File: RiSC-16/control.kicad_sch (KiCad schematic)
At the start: 4 parts, among them U16 74LS161, U17 74LS257, U18 74LS283

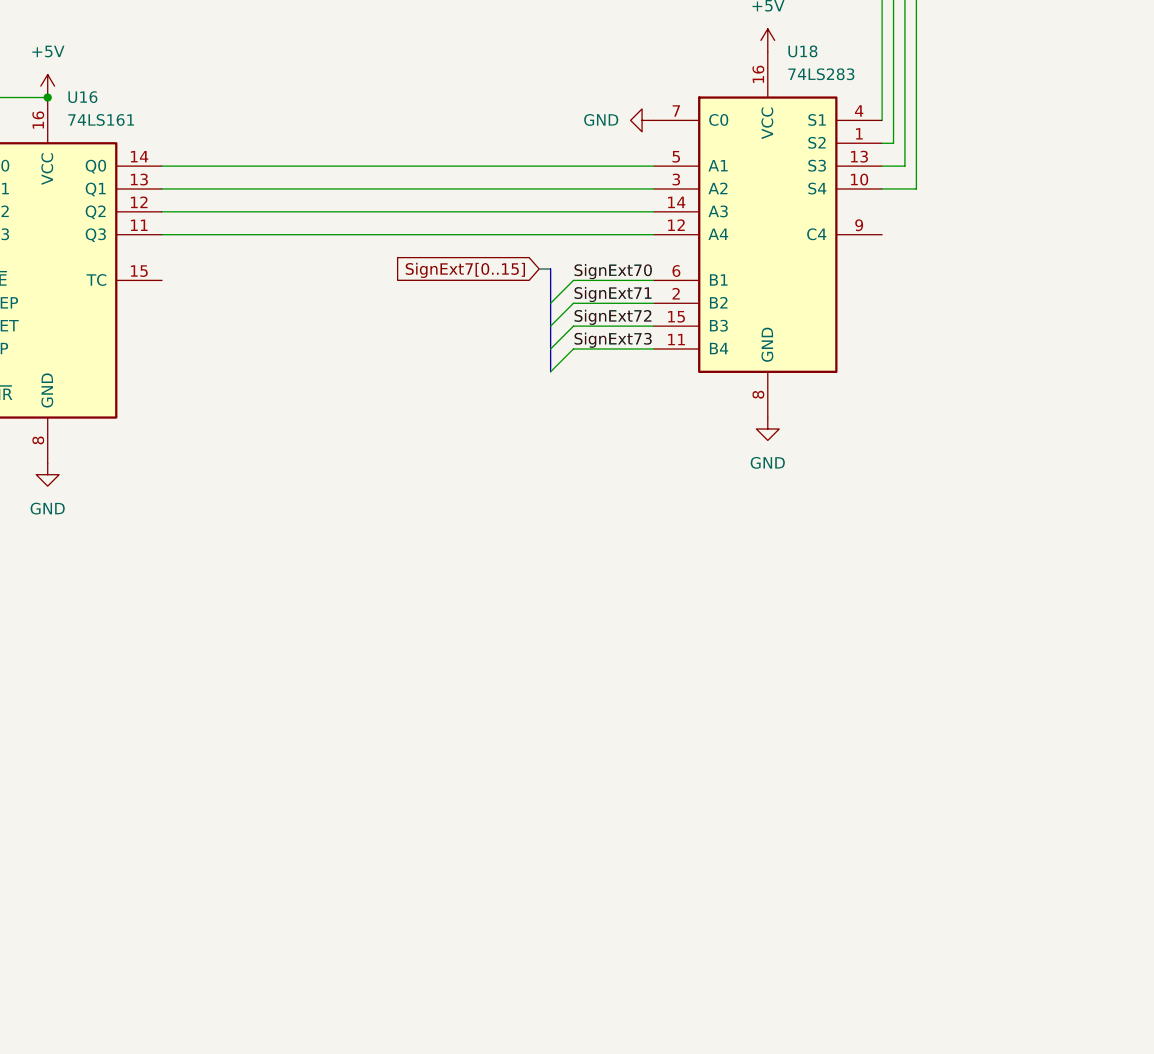
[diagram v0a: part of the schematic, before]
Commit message: Added program counter page.
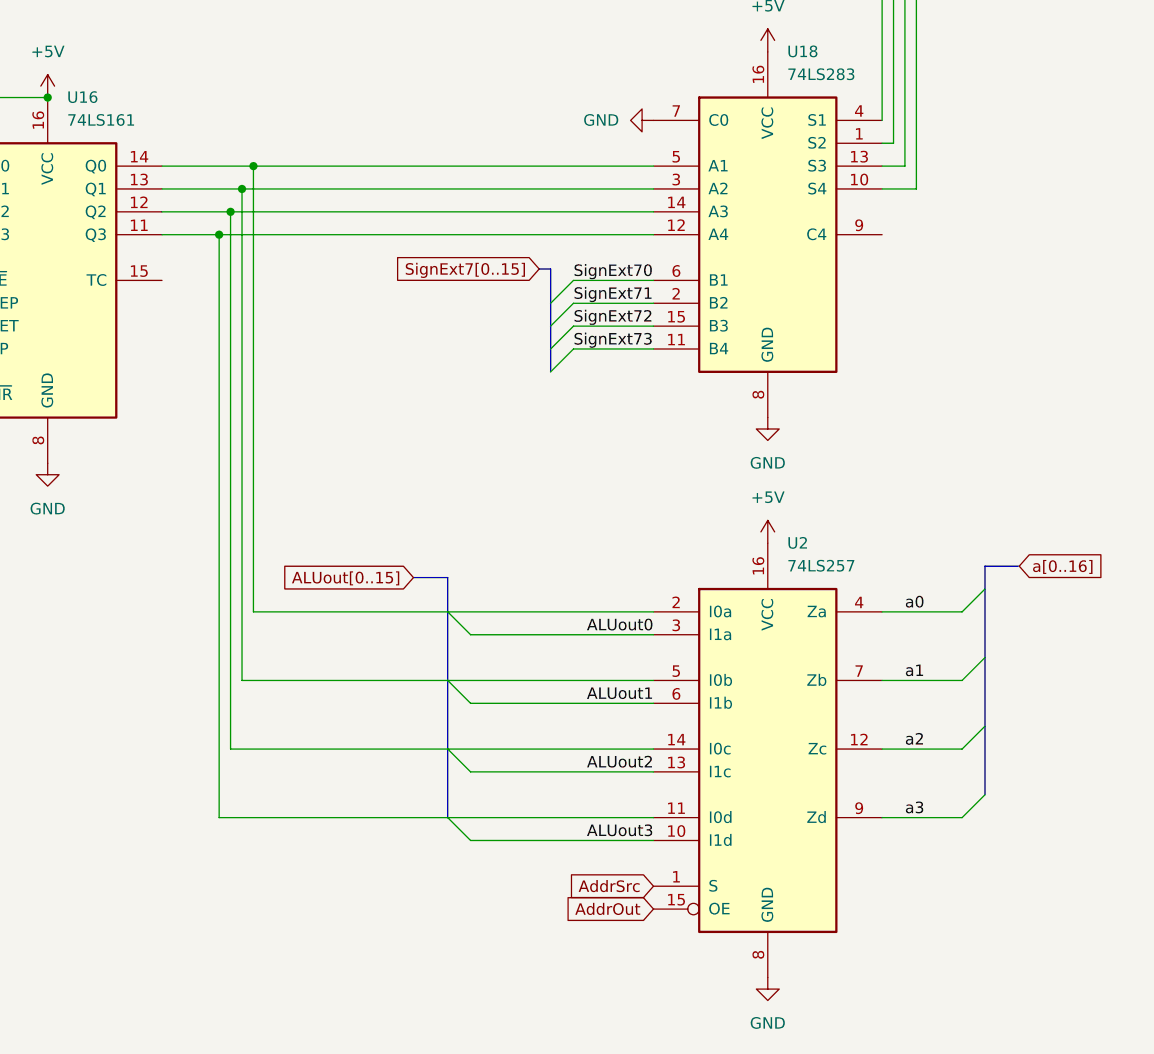
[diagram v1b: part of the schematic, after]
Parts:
- added U2: 74LS257, symbol 74xx:74LS257
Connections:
- net +5V: now also U2.16 (VCC)
- net ALUout0: now also U2.3 (I1a)
- net ALUout1: now also U2.6 (I1b)
- net ALUout2: now also U2.13 (I1c)
- net ALUout3: now also U2.10 (I1d)
- net GND: now also U2.8 (GND)
- net at U16.11 (Q3), U18.12 (A4): now also U2.11 (I0d)
- net at U16.12 (Q2), U18.14 (A3): now also U2.14 (I0c)
- net at U16.13 (Q1), U18.3 (A2): now also U2.5 (I0b)
- net at U16.14 (Q0), U18.5 (A1): now also U2.2 (I0a)
- new net AddrOut: U2.15 (OE)
- new net AddrSrc: U2.1 (S)
- new net a0: U2.4 (Za)
- new net a1: U2.7 (Zb)
- new net a2: U2.12 (Zc)
- new net a3: U2.9 (Zd)

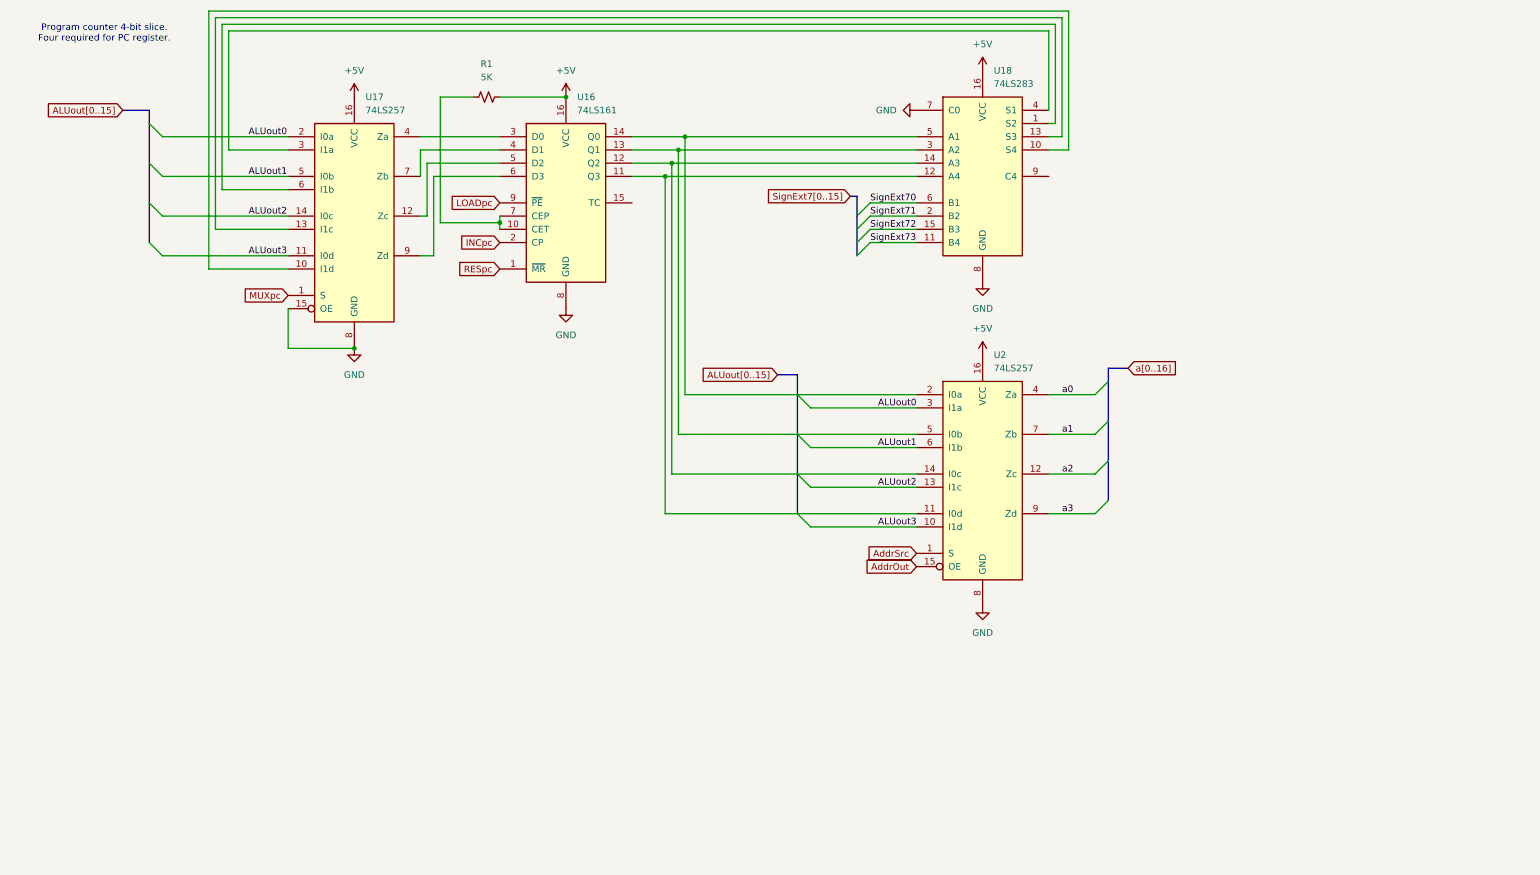
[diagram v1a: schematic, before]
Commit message: Move program ccounter to its own page
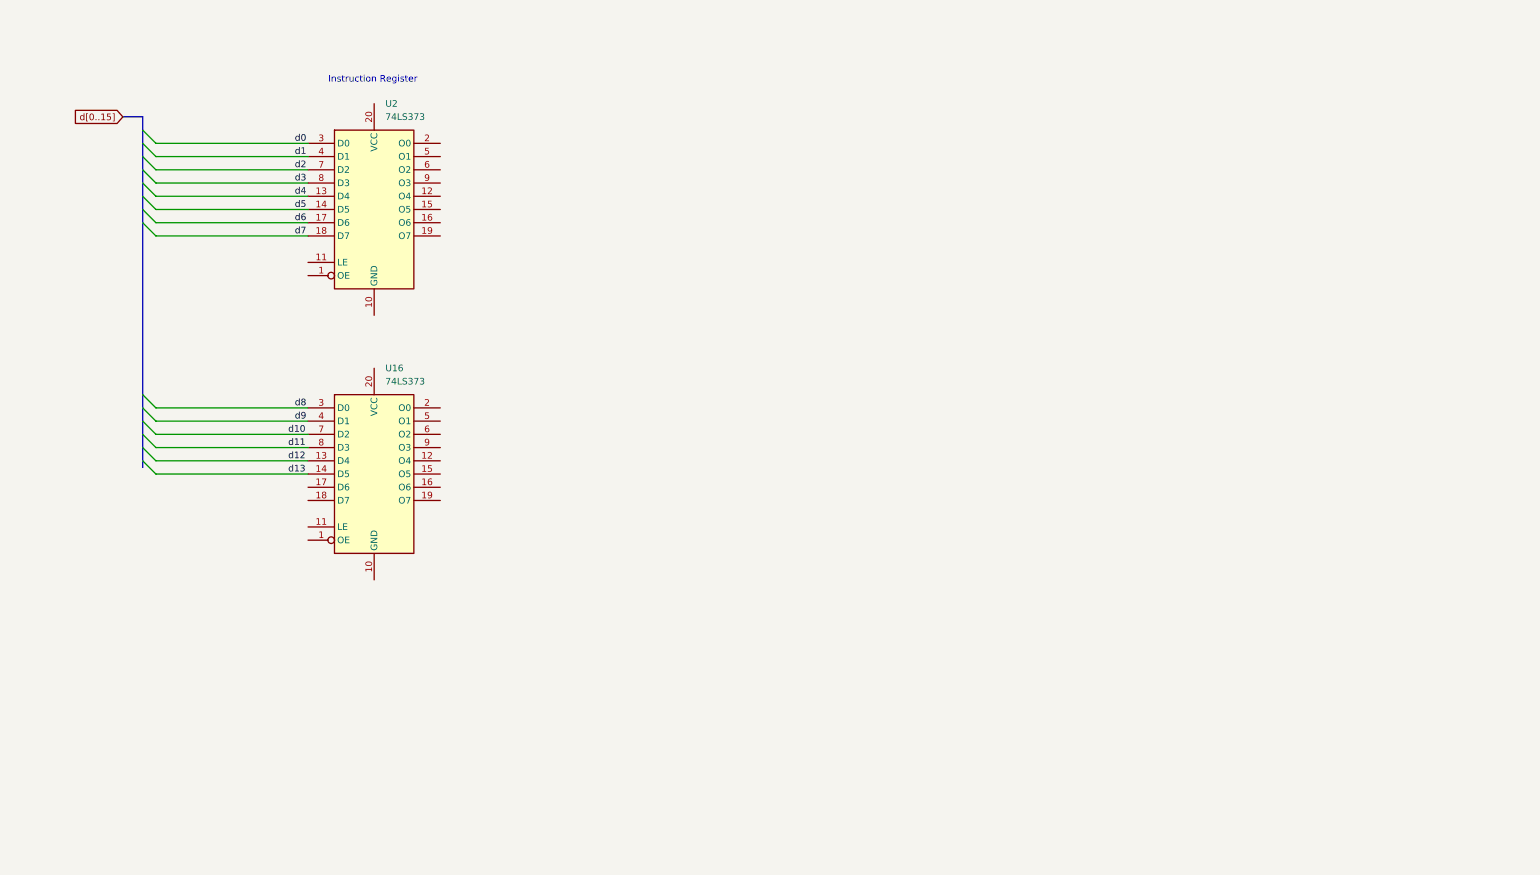
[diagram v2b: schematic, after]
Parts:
- removed R1: 5K, symbol Device:R_Small_US
- removed U16: 74LS161, symbol 74xx:74LS161
- removed U17, U2: 74LS257, symbol 74xx:74LS257
- removed U18: 74LS283, symbol 74xx:74LS283
- added U16, U2: 74LS373, symbol 74xx:74LS373
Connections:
- new net d0: U2.3 (D0)
- new net d1: U2.4 (D1)
- new net d10: U16.7 (D2)
- new net d11: U16.8 (D3)
- new net d12: U16.13 (D4)
- new net d13: U16.14 (D5)
- new net d2: U2.7 (D2)
- new net d3: U2.8 (D3)
- new net d4: U2.13 (D4)
- new net d5: U2.14 (D5)
- new net d6: U2.17 (D6)
- new net d7: U2.18 (D7)
- new net d8: U16.3 (D0)
- new net d9: U16.4 (D1)
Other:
- note added: "Instruction Register"
- note removed: "Program counter 4-bit slice. Four required for PC register."

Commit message: Added instruction register design.
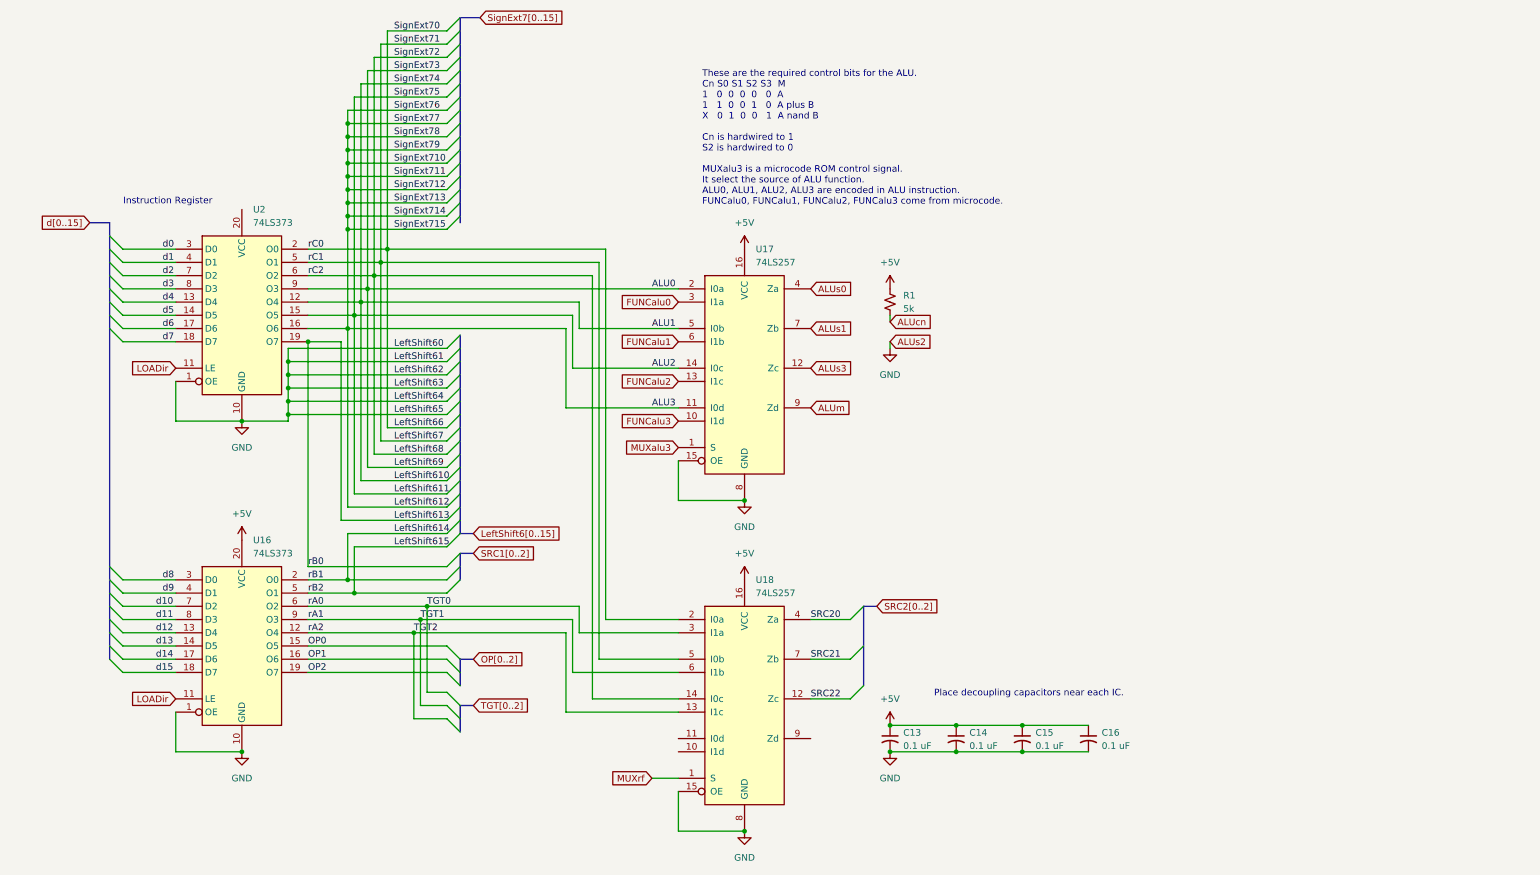
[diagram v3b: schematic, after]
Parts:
- added C13, C14, C15, C16: 0.1 uF, symbol Device:C_Small_US
- added R1: 5k, symbol Device:R_Small_US
- added U17, U18: 74LS257, symbol 74xx:74LS257
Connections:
- net GND: now reaches U16.1 (OE)
- net GND: now also U16.10 (GND), U2.1 (OE), U2.10 (GND), C13.2, C14.2, C15.2, C16.2, U17.15 (OE), U17.8 (GND), U18.15 (OE), U18.8 (GND)
- net LOADir: now reaches U16.11 (LE)
- net LOADir: now also U2.11 (LE)
- net TGT2: now reaches U16.12 (O4)
- net TGT2: now also U18.13 (I1c)
- net OP0: now reaches U16.15 (O5)
- net OP1: now reaches U16.16 (O6)
- net d14: now reaches U16.17 (D6)
- net d15: now reaches U16.18 (D7)
- net OP2: now reaches U16.19 (O7)
- net LeftShift614: now reaches U16.2 (O0)
- net +5V: now reaches U16.20 (VCC)
- net +5V: now also C13.1, C14.1, C15.1, C16.1, R1.1, U17.16 (VCC), U18.16 (VCC)
- net LeftShift615: now reaches U16.5 (O1)
- net TGT0: now reaches U16.6 (O2)
- net TGT0: now also U18.3 (I1a)
- net TGT1: now reaches U16.9 (O3)
- net TGT1: now also U18.6 (I1b)
- net ALU1: now reaches U2.12 (O4)
- net ALU1: now also U17.5 (I0b)
- net ALU2: now reaches U2.15 (O5)
- net ALU2: now also U17.14 (I0c)
- net ALU3: now reaches U2.16 (O6)
- net ALU3: now also U17.11 (I0d)
- net LeftShift613: now reaches U2.19 (O7)
- net LeftShift66: now reaches U2.2 (O0)
- net LeftShift66: now also U18.2 (I0a)
- net LeftShift67: now reaches U2.5 (O1)
- net LeftShift67: now also U18.5 (I0b)
- net LeftShift68: now reaches U2.6 (O2)
- net LeftShift68: now also U18.14 (I0c)
- net ALU0: now reaches U2.9 (O3)
- net ALU0: now also U17.2 (I0a)
- new net ALUcn: R1.2
- new net ALUm: U17.9 (Zd)
- new net ALUs0: U17.4 (Za)
- new net ALUs1: U17.7 (Zb)
- new net ALUs3: U17.12 (Zc)
- new net FUNCalu0: U17.3 (I1a)
- new net FUNCalu1: U17.6 (I1b)
- new net FUNCalu2: U17.13 (I1c)
- new net FUNCalu3: U17.10 (I1d)
- new net MUXalu3: U17.1 (S)
- new net MUXrf: U18.1 (S)
- new net SRC20: U18.4 (Za)
- new net SRC21: U18.7 (Zb)
- new net SRC22: U18.12 (Zc)
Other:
- note added: "Place decoupling capacitors near each IC."
- note added: "These are the required control bits for the ALU. Cn S0 S1 S2 S3 M 1 0 0 0 0 0 A 1 1 0 0 1 0 A plus B X 0 1 0 0 1 A nand B Cn is hardwired to 1 S2 is hardwired to 0 MUXalu3 is a microcode ROM control signal. It select the source of ALU function. ALU0, ALU1, ALU2, ALU3 are encoded in ALU instruction. FUNCalu0, FUNCalu1, FUNCalu2, FUNCalu3 come from microcode."
- moved on the sheet: U16, U2
